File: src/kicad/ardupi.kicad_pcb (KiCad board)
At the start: 2 copper layers, 65 x 30 mm, 12 parts, among them J1 GPIO_CONNECTOR, U2 ULN2803ADW, U3 MPU-9250, U4 PCA9685BS, U5 BMP280, U6 ADS1115IRUGR

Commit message: elec: PCA9685
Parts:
- removed the JP1 at (202.3, 92.0)
- added C_PCA1: 10uF, Capacitor_SMD:CP_Elec_8x5.4, F.Cu at (220.1, 107.3)
- added J2: Conn_02x16_Top_Bottom, Connector_PinHeader_2.54mm:PinHeader_2x16_P2.54mm_Vertical, F.Cu at (182.0, 61.5)
- added J3: Conn_01x16, Connector_PinHeader_2.54mm:PinHeader_1x16_P2.54mm_Vertical, F.Cu at (182.0, 54.3)
- added R1: 10K, Resistor_SMD:R_0805_2012Metric, F.Cu at (220.1, 94.6)
- added R10: 220 Ω, Resistor_SMD:R_0805_2012Metric, F.Cu at (187.1, 66.6)
- added R11: 220 Ω, Resistor_SMD:R_0805_2012Metric, F.Cu at (189.6, 66.6)
- added R12: 220 Ω, Resistor_SMD:R_0805_2012Metric, F.Cu at (192.2, 66.6)
- added R13: 220 Ω, Resistor_SMD:R_0805_2012Metric, F.Cu at (194.7, 66.6)
- added R14: 220 Ω, Resistor_SMD:R_0805_2012Metric, F.Cu at (197.2, 66.6)
- added R15: 220 Ω, Resistor_SMD:R_0805_2012Metric, F.Cu at (199.8, 66.6)
- added R16: 220 Ω, Resistor_SMD:R_0805_2012Metric, F.Cu at (202.3, 66.6)
- added R17: 220 Ω, Resistor_SMD:R_0805_2012Metric, F.Cu at (204.9, 66.6)
- added R18: 220 Ω, Resistor_SMD:R_0805_2012Metric, F.Cu at (207.4, 66.6)
- added R19: 220 Ω, Resistor_SMD:R_0805_2012Metric, F.Cu at (209.9, 66.6)
- added R2: 0 Ohm, Resistor_SMD:R_0805_2012Metric, F.Cu at (194.7, 99.6)
- added R20: 220 Ω, Resistor_SMD:R_0805_2012Metric, F.Cu at (212.5, 66.6)
- added R21: 220 Ω, Resistor_SMD:R_0805_2012Metric, F.Cu at (215.0, 66.6)
- added R22: 220 Ω, Resistor_SMD:R_0805_2012Metric, F.Cu at (217.6, 66.6)
- added R23: 220 Ω, Resistor_SMD:R_0805_2012Metric, F.Cu at (220.1, 66.6)
- added R3: 0 Ohm, Resistor_SMD:R_0805_2012Metric, F.Cu at (190.3, 102.6)
- added R4: 0 Ohm, Resistor_SMD:R_0805_2012Metric, F.Cu at (190.3, 99.6)
- added R5: 0 Ohm, Resistor_SMD:R_0805_2012Metric, F.Cu at (194.7, 102.6)
- added R6: 0 Ohm, Resistor_SMD:R_0805_2012Metric, F.Cu at (199.1, 102.6)
- added R7: 0 Ohm, Resistor_SMD:R_0805_2012Metric, F.Cu at (199.1, 99.6)
- added R8: 220 Ω, Resistor_SMD:R_0805_2012Metric, F.Cu at (182.0, 66.6)
- added R9: 220 Ω, Resistor_SMD:R_0805_2012Metric, F.Cu at (184.5, 66.6)
- moved JP1 54.6 mm to (237.9, 64.1)
- renumbered JP2 to JP1
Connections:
- J1 pad 3: /GPIO2_SDA1 -> /SDA1
- J1 pad 5: /GPIO3_SCL1 -> /SCL1
- JP1 pad 1: unconnected-(JP2-Pad1) -> /PWM1
- JP1 pad 10: unconnected-(JP2-Pad10) -> /PWM4
- JP1 pad 11: unconnected-(JP2-Pad11) -> /+V_SRVO
- JP1 pad 12: unconnected-(JP2-Pad12) -> GND
- JP1 pad 2: unconnected-(JP2-Pad2) -> /+V_SRVO
- JP1 pad 3: unconnected-(JP2-Pad3) -> GND
- JP1 pad 4: unconnected-(JP2-Pad4) -> /PWM2
- JP1 pad 5: unconnected-(JP2-Pad5) -> /+V_SRVO
- JP1 pad 6: unconnected-(JP2-Pad6) -> GND
- JP1 pad 7: unconnected-(JP2-Pad7) -> /PWM3
- JP1 pad 8: unconnected-(JP2-Pad8) -> /+V_SRVO
- JP1 pad 9: unconnected-(JP2-Pad9) -> GND
- U4 pad 1: unconnected-(U4-Pad1) -> Net-(U4-Pad1)
- U4 pad 10: unconnected-(U4-Pad10) -> Net-(U4-Pad10)
- U4 pad 12: unconnected-(U4-Pad12) -> Net-(U4-Pad12)
- U4 pad 13: unconnected-(U4-Pad13) -> Net-(U4-Pad13)
- U4 pad 14: unconnected-(U4-Pad14) -> Net-(U4-Pad14)
- U4 pad 15: unconnected-(U4-Pad15) -> Net-(U4-Pad15)
- U4 pad 16: unconnected-(U4-Pad16) -> Net-(U4-Pad16)
- U4 pad 17: unconnected-(U4-Pad17) -> Net-(U4-Pad17)
- U4 pad 18: unconnected-(U4-Pad18) -> Net-(U4-Pad18)
- U4 pad 19: unconnected-(U4-Pad19) -> Net-(U4-Pad19)
- U4 pad 2: unconnected-(U4-Pad2) -> Net-(R6-Pad1)
- U4 pad 20: unconnected-(U4-Pad20) -> Net-(R1-Pad1)
- U4 pad 21: unconnected-(U4-Pad21) -> Net-(R7-Pad1)
- U4 pad 22: unconnected-(U4-Pad22) -> GND
- U4 pad 23: unconnected-(U4-Pad23) -> /SDA1
- U4 pad 24: unconnected-(U4-Pad24) -> /SCL1
- U4 pad 25: unconnected-(U4-Pad25) -> +5V
- U4 pad 26: unconnected-(U4-Pad26) -> Net-(R2-Pad1)
- U4 pad 27: unconnected-(U4-Pad27) -> Net-(R3-Pad1)
- U4 pad 28: unconnected-(U4-Pad28) -> Net-(R4-Pad1)
- U4 pad 3: unconnected-(U4-Pad3) -> Net-(U4-Pad3)
- U4 pad 4: unconnected-(U4-Pad4) -> Net-(U4-Pad4)
- U4 pad 5: unconnected-(U4-Pad5) -> Net-(U4-Pad5)
- U4 pad 6: unconnected-(U4-Pad6) -> Net-(U4-Pad6)
- U4 pad 7: unconnected-(U4-Pad7) -> Net-(U4-Pad7)
- U4 pad 8: unconnected-(U4-Pad8) -> Net-(U4-Pad8)
- U4 pad 9: unconnected-(U4-Pad9) -> Net-(U4-Pad9)

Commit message: elec: baro & imu
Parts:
- added C1: 0.1uF, Capacitor_SMD:C_0201_0603Metric_Pad0.64x0.40mm_HandSolder, F.Cu at (232.2, 115.5)
- added C2: 1uF, Capacitor_SMD:C_0201_0603Metric_Pad0.64x0.40mm_HandSolder, F.Cu at (232.2, 116.6)
- added C3: 0.1uF, Capacitor_SMD:C_0201_0603Metric_Pad0.64x0.40mm_HandSolder, F.Cu at (196.0, 140.3)
- added C4: 0.01uF, Capacitor_SMD:C_0201_0603Metric_Pad0.64x0.40mm_HandSolder, F.Cu at (195.2, 143.6)
- added C5: 1uF, Capacitor_SMD:C_0201_0603Metric_Pad0.64x0.40mm_HandSolder, F.Cu at (196.0, 138.5)
- added R24: 4.7KΩ, Resistor_SMD:R_0603_1608Metric_Pad0.98x0.95mm_HandSolder, F.Cu at (240.4, 117.4)
- added R25: 4.7KΩ, Resistor_SMD:R_0603_1608Metric_Pad0.98x0.95mm_HandSolder, F.Cu at (240.4, 120.4)
- added R26: 10KΩ, Resistor_SMD:R_0603_1608Metric_Pad0.98x0.95mm_HandSolder, F.Cu at (236.0, 120.4)
- added R27: 4.7KΩ, Resistor_SMD:R_0603_1608Metric_Pad0.98x0.95mm_HandSolder, F.Cu at (236.0, 117.4)
- added R28: 10KΩ, Resistor_SMD:R_0603_1608Metric_Pad0.98x0.95mm_HandSolder, F.Cu at (191.6, 144.1)
- added R29: 4.7KΩ, Resistor_SMD:R_0603_1608Metric_Pad0.98x0.95mm_HandSolder, F.Cu at (187.2, 144.1)
- added R30: 4.7KΩ, Resistor_SMD:R_0603_1608Metric_Pad0.98x0.95mm_HandSolder, F.Cu at (192.4, 138.9)
- added R31: 10KΩ, Resistor_SMD:R_0603_1608Metric_Pad0.98x0.95mm_HandSolder, F.Cu at (192.4, 141.4)
- added U1: MPU-9250, Sensor_Motion:InvenSense_QFN-24_3x3mm_P0.4mm, F.Cu at (187.6, 140.2)
- moved R23 124.0 mm to (118.5, 137.7), turned to 90 degrees
- moved R22 119.7 mm to (121.1, 137.6), turned to 90 degrees
- moved R21 115.7 mm to (123.7, 137.6), turned to 90 degrees
- moved R20 111.7 mm to (126.2, 137.6), turned to 90 degrees
- moved R19 107.9 mm to (128.7, 137.6), turned to 90 degrees
- moved R18 104.1 mm to (131.3, 137.6), turned to 90 degrees
- moved R17 100.4 mm to (133.8, 137.6), turned to 90 degrees
- moved J3 96.9 mm to (156.6, 147.9), turned to -90 degrees
- moved R16 96.9 mm to (136.4, 137.6), turned to 90 degrees
- moved R15 93.5 mm to (138.9, 137.6), turned to 90 degrees
- moved R14 90.3 mm to (141.4, 137.6), turned to 90 degrees
- moved R13 87.2 mm to (144.0, 137.6), turned to 90 degrees
- moved J2 85.0 mm to (156.7, 142.7), turned to -90 degrees
- moved R12 84.4 mm to (146.5, 137.6), turned to 90 degrees
- moved U4 82.0 mm to (128.7, 127.6), turned to -90 degrees
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- renumbered U5 to BMP280
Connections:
- BMP280 pad 1: unconnected-(U5-Pad1) -> GND
- BMP280 pad 2: unconnected-(U5-Pad2) -> /SPI_CE1_N
- BMP280 pad 3: unconnected-(U5-Pad3) -> /SPI_MOSI
- BMP280 pad 4: unconnected-(U5-Pad4) -> /SPI_SCLK
- BMP280 pad 5: unconnected-(U5-Pad5) -> /SPI_MISO
- BMP280 pad 6: unconnected-(U5-Pad6) -> /+3.3V
- BMP280 pad 7: unconnected-(U5-Pad7) -> GND
- BMP280 pad 8: unconnected-(U5-Pad8) -> /+3.3V
- J1 pad 19: /GPIO10_SPI_MOSI -> /SPI_MOSI
- J1 pad 21: /GPIO9_SPI_MISO -> /SPI_MISO
- J1 pad 23: /GPIO11_SPI_SCLK -> /SPI_SCLK
- J1 pad 24: /GPIO8_SPI_CE0_N -> /SPI_CE0_N
- J1 pad 26: /GPIO7_SPI_CE1_N -> /SPI_CE1_N
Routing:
- net /PWM13: track 0.00 -> 8.08 mm
- net /PWM11: track 0.00 -> 7.92 mm
- net /PWM10: track 0.00 -> 7.76 mm
- net /PWM16: track 0.00 -> 7.70 mm
- net /PWM4: track 0.00 -> 7.68 mm
- net /PWM14: track 0.00 -> 7.68 mm
- net /PWM9: track 0.00 -> 7.68 mm
- net /PWM8: track 0.00 -> 7.68 mm
- net /PWM7: track 0.00 -> 7.68 mm
- net /PWM6: track 0.00 -> 7.68 mm
- net /PWM5: track 0.00 -> 7.68 mm
- net /PWM3: track 0.00 -> 7.68 mm
- net /PWM2: track 0.00 -> 7.68 mm
- net /PWM15: track 0.00 -> 7.68 mm
- net /PWM12: track 0.00 -> 7.68 mm
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
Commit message: clean layout
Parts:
- removed R18, R19, R20, R21, R22, R23: 220 Ω, Resistor_SMD:R_0805_2012Metric
- removed U3: MPU-9250, mpu9250:mpu9250
- added C6: 10uF, Capacitor_SMD:C_0402_1005Metric, F.Cu at (231.7, 137.6)
- added J4: Conn_01x04, Connector_JST:JST_EH_B4B-EH-A_1x04_P2.50mm_Vertical, F.Cu at (199.3, 132.5)
- added J5: Conn_01x05, Connector_JST:JST_EH_B5B-EH-A_1x05_P2.50mm_Vertical, F.Cu at (199.3, 126.6)
- added J6: Conn_01x06, Connector_JST:JST_EH_B6B-EH-A_1x06_P2.50mm_Vertical, F.Cu at (199.3, 114.9)
- added J7: Conn_01x04, Connector_JST:JST_EH_B4B-EH-A_1x04_P2.50mm_Vertical, F.Cu at (199.3, 138.3)
- added J8: Conn_01x02, Connector_JST:JST_EH_B2B-EH-A_1x02_P2.50mm_Vertical, F.Cu at (218.9, 114.9)
- added J9: Conn_01x04, Connector_JST:JST_EH_B4B-EH-A_1x04_P2.50mm_Vertical, F.Cu at (216.4, 128.4)
- added JP2: PWM-HEADER-3X04, Ardupi:PWM-Header-3x4, F.Cu at (246.3, 120.7)
- added R34: 10KΩ, Resistor_SMD:R_0402_1005Metric, F.Cu at (219.5, 122.8)
- added R35: 10KΩ, Resistor_SMD:R_0402_1005Metric, F.Cu at (208.9, 142.5)
- added R36: 10KΩ, Resistor_SMD:R_0402_1005Metric, F.Cu at (220.1, 124.8)
- added R37: 10KΩ, Resistor_SMD:R_0402_1005Metric, F.Cu at (225.9, 134.6)
- C1, C2, C3, C4, C5: footprint Capacitor_SMD:C_0201_0603Metric_Pad0.64x0.40mm_HandSolder -> Capacitor_SMD:C_0402_1005Metric
- J2: value Conn_02x16_Top_Bottom -> Conn_01x10; footprint Connector_PinHeader_2.54mm:PinHeader_2x16_P2.54mm_Vertical -> Connector_JST:JST_EH_B10B-EH-A_1x10_P2.50mm_Vertical
- J3: value Conn_01x16 -> Conn_01x05; footprint Connector_PinHeader_2.54mm:PinHeader_1x16_P2.54mm_Vertical -> Connector_JST:JST_EH_B5B-EH-A_1x05_P2.50mm_Vertical
- JP1: value HEADER-3X04 -> PWM-HEADER-3X04; footprint Adafruit PCA9685 rev C:3X04 -> Ardupi:PWM-Header-3x4
- R1, R10, R11, R12, R13, R14, R15, R16, R17: footprint Resistor_SMD:R_0805_2012Metric -> Resistor_SMD:R_0402_1005Metric
- R2, R6, R7: value 0 Ohm -> 10k; footprint Resistor_SMD:R_0805_2012Metric -> Resistor_SMD:R_0402_1005Metric
- R24, R25, R26, R27, R28, R29, R30, R31: footprint Resistor_SMD:R_0603_1608Metric_Pad0.98x0.95mm_HandSolder -> Resistor_SMD:R_0402_1005Metric
- R3, R4, R5: value 0 Ohm -> 10K; footprint Resistor_SMD:R_0805_2012Metric -> Resistor_SMD:R_0402_1005Metric
- R8, R9: value 220 Ω -> 470k; footprint Resistor_SMD:R_0805_2012Metric -> Resistor_SMD:R_0402_1005Metric
- U6: footprint ADS1115IRUGR:ADS1115IRUGR -> Ardupi:ADS1115IRUGR
- moved U4 129.1 mm to (256.6, 110.6), turned to 0 degrees
- moved R16 87.6 mm to (223.1, 124.8), turned to 0 degrees
- moved R15 86.7 mm to (223.6, 119.1), turned to 0 degrees
- moved R14 84.6 mm to (225.9, 142.6), turned to 0 degrees
- moved R12 82.3 mm to (228.8, 139.6), turned to 0 degrees
- moved R13 79.0 mm to (223.0, 137.6), turned to 0 degrees
- moved R9 77.6 mm to (231.7, 135.6), turned to 0 degrees
- moved C4 76.1 mm to (262.2, 107.4)
- moved R11 74.1 mm to (223.0, 142.6), turned to 0 degrees
- moved JP1 71.2 mm to (233.1, 130.2)
- moved R28 67.4 mm to (253.4, 117.3)
- moved R17 66.5 mm to (200.2, 142.5), turned to 0 degrees
- moved R8 66.3 mm to (223.0, 135.6), turned to 0 degrees
- moved R10 64.1 mm to (214.3, 124.3), turned to 0 degrees
- moved J2 54.3 mm to (199.3, 109.1), turned to 0 degrees
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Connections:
- J2 pad 1: Net-(J2-Pad1) -> GND
- J2 pad 10: /PWM5 -> /RC8
- J2 pad 2: /PWM1 -> +5V
- J2 pad 3: Net-(J2-Pad1) -> /RC1
- J2 pad 4: /PWM2 -> /RC2
- J2 pad 5: Net-(J2-Pad1) -> /RC3
- J2 pad 6: /PWM3 -> /RC4
- J2 pad 7: Net-(J2-Pad1) -> /RC5
- J2 pad 8: /PWM4 -> /RC6
- J2 pad 9: Net-(J2-Pad1) -> /RC7
- J3 pad 1: Net-(J3-Pad1) -> GND
- J3 pad 2: Net-(J3-Pad1) -> +5V
- J3 pad 3: Net-(J3-Pad1) -> /MOSI
- J3 pad 4: Net-(J3-Pad1) -> /MISO
- J3 pad 5: Net-(J3-Pad1) -> /SCLK
- JP1 pad 1: /PWM1 -> Net-(JP1-Pad1)
- JP1 pad 10: /PWM4 -> Net-(JP1-Pad10)
- JP1 pad 11: /+V_SRVO -> +5V
- JP1 pad 2: /+V_SRVO -> +5V
- JP1 pad 4: /PWM2 -> Net-(JP1-Pad4)
- JP1 pad 5: /+V_SRVO -> +5V
- JP1 pad 7: /PWM3 -> Net-(JP1-Pad7)
- JP1 pad 8: /+V_SRVO -> +5V
- R10 pad 1: /PWM3 -> Net-(JP1-Pad1)
- R10 pad 2: Net-(R10-Pad2) -> /PWM1
- R11 pad 1: /PWM4 -> Net-(JP1-Pad4)
- R11 pad 2: Net-(R11-Pad2) -> /PWM2
- R12 pad 1: /PWM5 -> Net-(JP1-Pad7)
- R12 pad 2: Net-(R12-Pad2) -> /PWM3
- R13 pad 1: /PWM6 -> Net-(JP1-Pad10)
- R13 pad 2: Net-(R13-Pad2) -> /PWM4
- R14 pad 1: /PWM7 -> Net-(JP2-Pad1)
- R14 pad 2: Net-(R14-Pad2) -> /PWM5
- R15 pad 1: /PWM8 -> Net-(JP2-Pad4)
- R15 pad 2: Net-(R15-Pad2) -> /PWM6
- R16 pad 1: /PWM9 -> Net-(JP2-Pad7)
- R16 pad 2: Net-(R16-Pad2) -> /PWM7
- R17 pad 1: /PWM10 -> Net-(JP2-Pad10)
- R17 pad 2: Net-(R17-Pad2) -> /PWM8
- R8 pad 1: /PWM1 -> +5V
- R8 pad 2: Net-(R8-Pad2) -> Net-(J8-Pad2)
- R9 pad 1: /PWM2 -> /PCA_EN
- R9 pad 2: Net-(R9-Pad2) -> Net-(J8-Pad2)
- U2 pad 1: unconnected-(U2-Pad1) -> /BUZZER
- U2 pad 10: unconnected-(U2-Pad10) -> /V_EXT
- U2 pad 11: unconnected-(U2-Pad11) -> /LED3_OUT
- U2 pad 12: unconnected-(U2-Pad12) -> /LED3_OUT
- U2 pad 13: unconnected-(U2-Pad13) -> /LED2_OUT
- U2 pad 14: unconnected-(U2-Pad14) -> /LED2_OUT
- U2 pad 15: unconnected-(U2-Pad15) -> /LED1_OUT
- U2 pad 16: unconnected-(U2-Pad16) -> /LED1_OUT
- U2 pad 17: unconnected-(U2-Pad17) -> /BUZZER_OUT
- U2 pad 18: unconnected-(U2-Pad18) -> /BUZZER_OUT
- U2 pad 2: unconnected-(U2-Pad2) -> /BUZZER
- U2 pad 3: unconnected-(U2-Pad3) -> /LED1
- U2 pad 4: unconnected-(U2-Pad4) -> /LED1
- U2 pad 5: unconnected-(U2-Pad5) -> /LED2
- U2 pad 6: unconnected-(U2-Pad6) -> /LED2
- U2 pad 7: unconnected-(U2-Pad7) -> /LED3
- U2 pad 8: unconnected-(U2-Pad8) -> /LED3
- U2 pad 9: unconnected-(U2-Pad9) -> GND
- U4 pad 10: Net-(R15-Pad2) -> /PWM8
- U4 pad 12: Net-(R16-Pad2) -> /PWM9
- U4 pad 13: Net-(R17-Pad2) -> /PWM10
- U4 pad 14: Net-(R18-Pad2) -> /PWM11
- U4 pad 15: Net-(R19-Pad2) -> /PWM12
- U4 pad 16: Net-(R20-Pad2) -> /PWM13
- U4 pad 17: Net-(R21-Pad2) -> /PWM14
- U4 pad 18: Net-(R22-Pad2) -> /PWM15
- U4 pad 19: Net-(R23-Pad2) -> /PWM16
- U4 pad 3: Net-(R8-Pad2) -> /PWM1
- U4 pad 4: Net-(R9-Pad2) -> /PWM2
- U4 pad 5: Net-(R10-Pad2) -> /PWM3
- U4 pad 6: Net-(R11-Pad2) -> /PWM4
- U4 pad 7: Net-(R12-Pad2) -> /PWM5
- U4 pad 8: Net-(R13-Pad2) -> /PWM6
- U4 pad 9: Net-(R14-Pad2) -> /PWM7
- U6 pad 1: unconnected-(U6-Pad1) -> Net-(R34-Pad2)
- U6 pad 10: unconnected-(U6-Pad10) -> Net-(R36-Pad1)
- U6 pad 4: unconnected-(U6-Pad4) -> /AIO1
- U6 pad 5: unconnected-(U6-Pad5) -> /AIO2
- U6 pad 6: unconnected-(U6-Pad6) -> /AIO3
- U6 pad 9: unconnected-(U6-Pad9) -> Net-(R37-Pad1)
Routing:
- net /PWM13: track 8.08 -> 0.00 mm
- net /PWM11: track 7.92 -> 0.00 mm
- net /PWM10: track 7.76 -> 0.00 mm
- net /PWM16: track 7.70 -> 0.00 mm
- net /PWM4: track 7.68 -> 0.00 mm
- net /PWM14: track 7.68 -> 0.00 mm
- net /PWM9: track 7.68 -> 0.00 mm
- net /PWM8: track 7.68 -> 0.00 mm
- net /PWM7: track 7.68 -> 0.00 mm
- net /PWM6: track 7.68 -> 0.00 mm
- net /PWM5: track 7.68 -> 0.00 mm
- net /PWM3: track 7.68 -> 0.00 mm
- net /PWM2: track 7.68 -> 0.00 mm
- net /PWM15: track 7.68 -> 0.00 mm
- net /PWM12: track 7.68 -> 0.00 mm
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
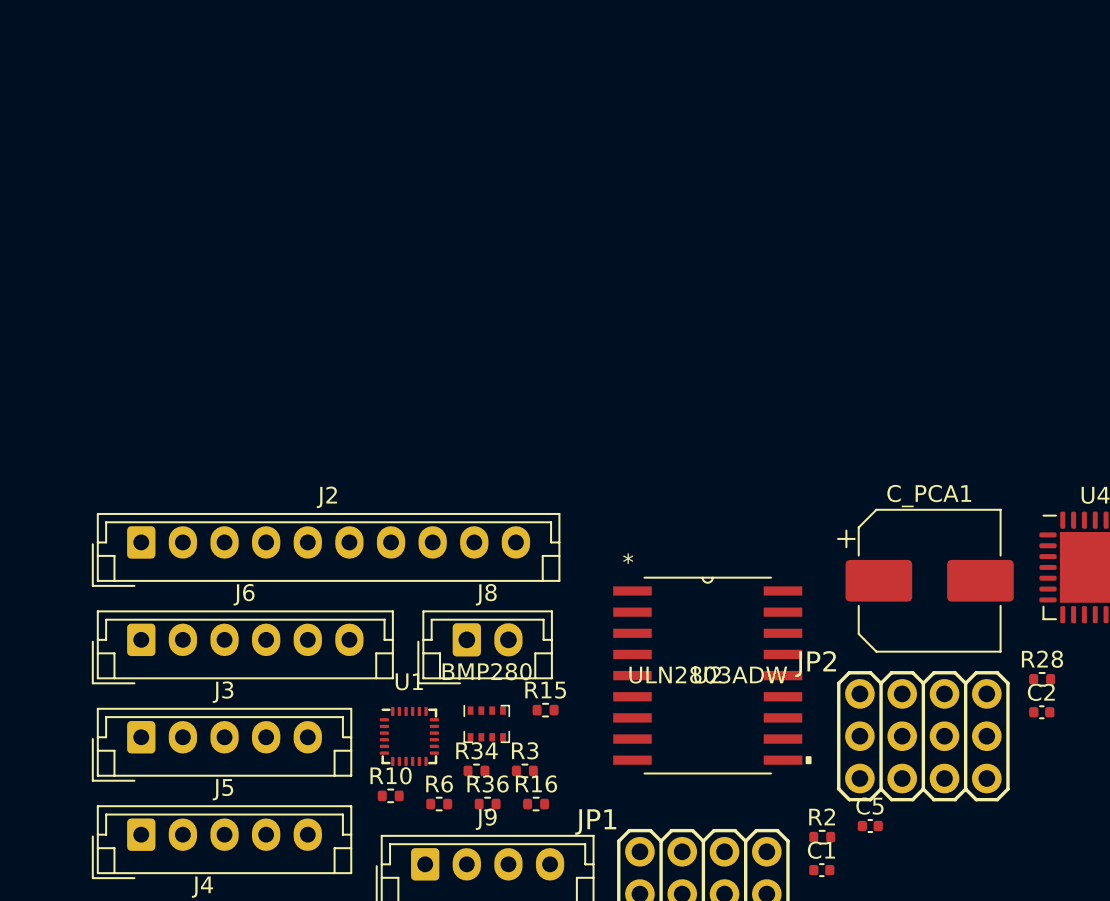
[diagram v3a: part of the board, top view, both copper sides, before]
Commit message: +3x8 PWM header
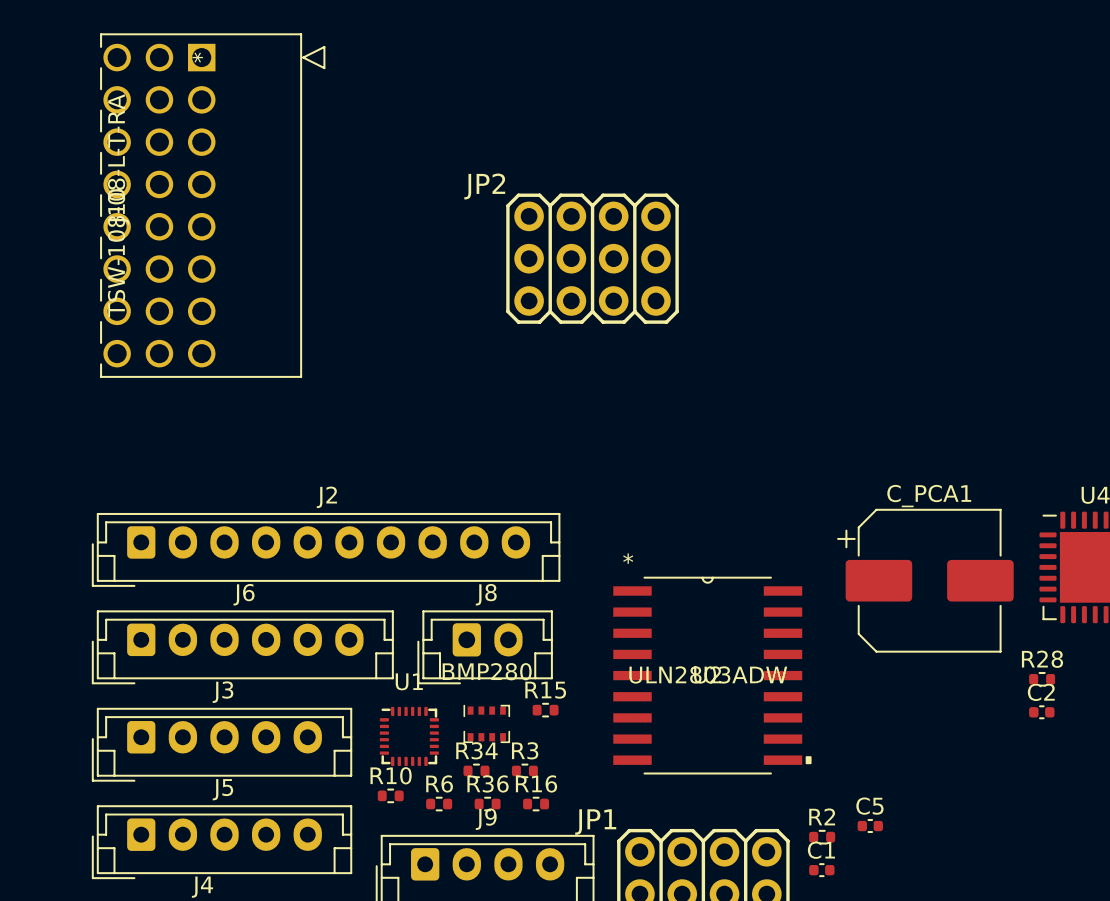
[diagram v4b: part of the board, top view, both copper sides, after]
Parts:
- added J10: TSW-108-08-L-T-RA, Ardupi:TSW-108-08-L-T-RA, F.Cu at (203.0, 80.0)
- moved JP2 34.9 mm to (226.4, 92.0)
